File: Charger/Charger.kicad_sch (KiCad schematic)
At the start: 4 parts, among them J1 Bat_ballanser_conn, J2 Battery_conn, J3 Power_conn, J4 Screen_SPInCtrlnPwr_Conn

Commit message: Schematic trace update
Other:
- sheet MCU ports: added +3.3V; removed none
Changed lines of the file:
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@@
+		)
+	)
+	(wire
+		(pts
+			(xy 134.62 30.48) (xy 134.62 33.02)
+		)
+		(stroke
+			(width 0)
+			(type default)
 		)
 	)
@@
 		)
 	)
+	(symbol
+		(lib_id "power:+3.3V")
+		(at 134.62 30.48 0)
+		(unit 1)
+		(exclude_from_sim no)
+		(in_bom yes)
+		(on_board yes)
+		(dnp no)
+		(property "Reference" "#PWR067"
+			(at 134.62 34.29 0)
+			(effects
+				(font
+					(size 1.27 1.27)
+				)
+				(hide yes)
+			)
+		)
+		(property "Value" "+3.3V"
+			(at 134.62 26.67 0)
+			(effects
+				(font
+					(size 1.27 1.27)
+				)
+			)
+		)
+		(property "Footprint" ""
+			(at 134.62 30.48 0)
+			(effects
+				(font
+					(size 1.27 1.27)
+				)
+				(hide yes)
+			)
+		)
+		(property "Datasheet" ""
+			(at 134.62 30.48 0)
+			(effects
+				(font
+					(size 1.27 1.27)
+				)
+				(hide yes)
+			)
+		)
+		(property "Description" "Power symbol creates a global label with name \"+3.3V\""
+			(at 134.62 30.48 0)
+			(effects
+				(font
+					(size 1.27 1.27)
+				)
+				(hide yes)
+			)
+		)
+		(pin "1"
+		)
+		(instances
+			(project "Charger"
+				(path "/f0501846-9b00-4ec1-8596-952177c35a04"
+					(reference "#PWR067")
+					(unit 1)
+				)
+			)
+		)
+	)
 	(sheet
 		(at 214.63 114.3)
@@
 		(at 119.38 33.02)
 		(size 45.72 73.66)
-		(fields_autoplaced yes)
 		(stroke
 			(width 0.1524)
@@
 		)
 		(property "Sheetname" "MCU"
-			(at 119.38 32.3084 0)
-			(effects
-				(font
-					(size 1.27 1.27)
+			(at 139.954 71.12 0)
+			(effects
+				(font
+					(size 1.27 1.27)
+					(bold yes)
 				)
 				(justify left bottom)
@@
 			(effects
 				(font
+					(size 1.27 1.27)
+				)
+				(justify right)
+			)
+		)
+		(pin "+3.3V" input
+			(at 134.62 33.02 90)
+			(effects
+				(font

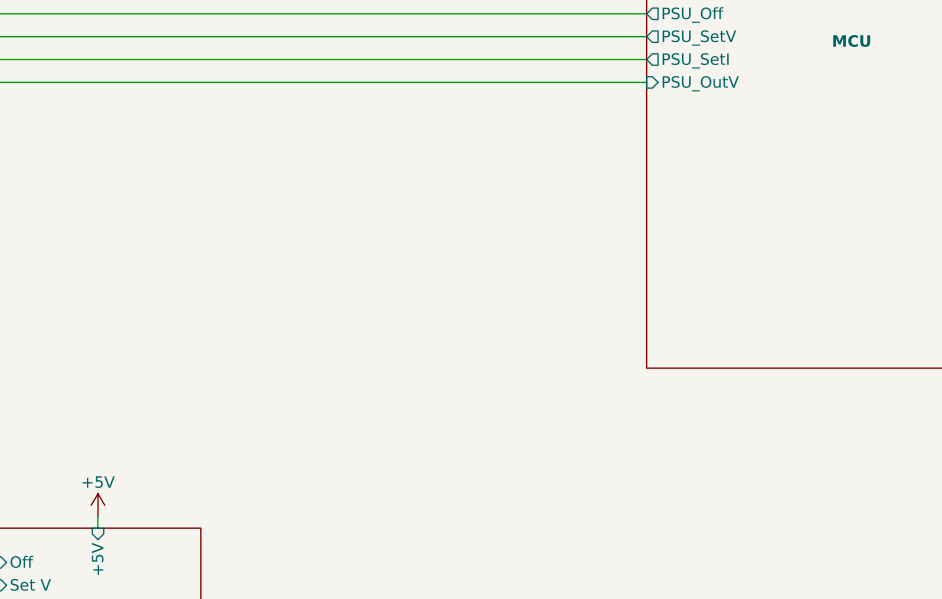
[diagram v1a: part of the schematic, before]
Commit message: Semi finished pinning the mcu and added ui pins
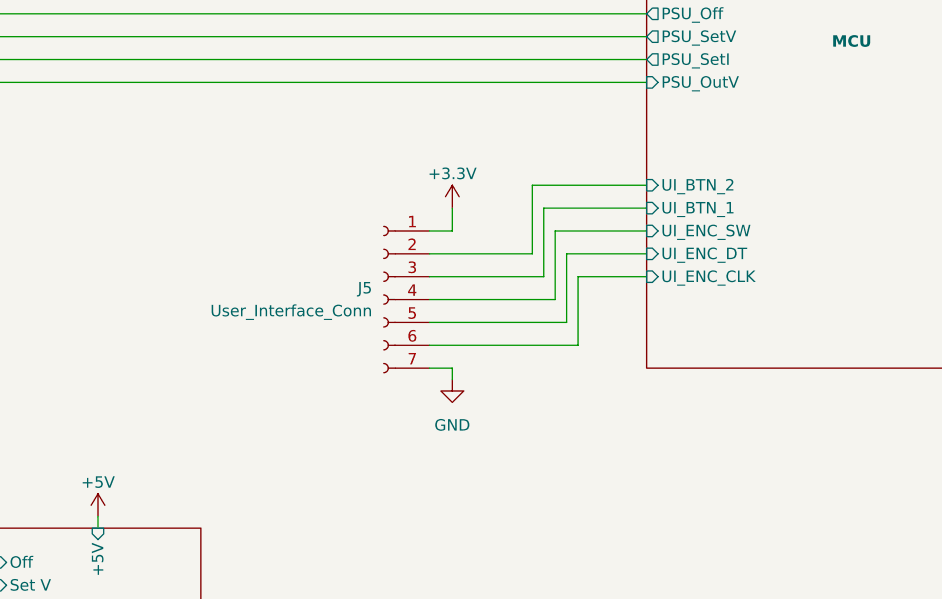
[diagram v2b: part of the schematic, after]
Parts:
- added J5: User_Interface_Conn, Connector_PinHeader_2.54mm:PinHeader_1x07_P2.54mm_Horizontal, symbol Connector:Conn_01x07_Socket
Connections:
- net +3.3V: now also J5.1 (Pin_1)
- net GND: now also J5.7 (Pin_7)
- new net MCU/UI_BTN_1: J5.3 (Pin_3)
- new net MCU/UI_BTN_2: J5.2 (Pin_2)
- new net MCU/UI_ENC_CLK: J5.6 (Pin_6)
- new net MCU/UI_ENC_DT: J5.5 (Pin_5)
- new net MCU/UI_ENC_SW: J5.4 (Pin_4)
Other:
- sheet MCU ports: added UI_BTN_1, UI_BTN_2, UI_ENC_CLK, UI_ENC_DT, UI_ENC_SW; removed none

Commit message: przegląd
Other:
- note added: "to jest załączenie baterii nie pomiaru"
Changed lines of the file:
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@@
+		)
+	)
+	(text "to jest załączenie baterii nie pomiaru \n"
+		(exclude_from_sim no)
+		(at 184.658 104.902 0)
+		(effects
+			(font
+				(size 1.27 1.27)
+			)
 		)
 	)

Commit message: Notes after design meeting
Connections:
- no-connect marks 0 -> 1
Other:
- note removed: "Co robi FM? xD"
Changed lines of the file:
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@@
 		(color 0 0 0 0)
+	)
+	(no_connect
+		(at 175.26 55.88)
 	)
 	(wire
@@
 		(effects
 			(font
-				(size 1.27 1.27)
-			)
-		)
-	)
-	(text "Co robi FM? xD"
-		(exclude_from_sim no)
-		(at 188.468 56.134 0)
-		(effects
-			(font

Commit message: UPDATE UC
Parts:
- added J7: Temp_Sens_Conn, Connector_PinHeader_2.54mm:PinHeader_1x02_P2.54mm_Vertical, symbol Connector:Conn_01x02_Socket
- J4: footprint (none) -> Connector_PinHeader_2.54mm:PinHeader_1x10_P2.54mm_Vertical
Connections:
- net GND: now also J7.1 (Pin_1)
- new net MCU/ONE_WIRE: J7.2 (Pin_2)
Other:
- sheet MCU ports: added BAT_P_ON, ONE_WIRE, PSU_OutI; removed ISENS_EN
- note added: "tu by chciały być magistrale"
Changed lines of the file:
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@@
 	(paper "A4")
 	(junction
+		(at 36.83 135.89)
+		(diameter 0)
+		(color 0 0 0 0)
+	)
+	(junction
 		(at 212.09 132.08)
 		(diameter 0)
@@
 	(wire
 		(pts
+			(xy 105.41 55.88) (xy 105.41 58.42)
+		)
+		(stroke
+			(width 0)
+			(type default)
+		)
+	)
+	(wire
+		(pts
 			(xy 171.45 35.56) (xy 175.26 35.56)
 		)
@@
 	(wire
 		(pts
+			(xy 119.38 77.47) (xy 27.94 77.47)
+		)
+		(stroke
+			(width 0)
+			(type default)
+		)
+	)
+	(wire
+		(pts
 			(xy 95.25 106.68) (xy 97.79 106.68)
 		)
@@
 	(wire
 		(pts
+			(xy 27.94 135.89) (xy 36.83 135.89)
+		)
+		(stroke
+			(width 0)
+			(type default)
+		)
+	)
+	(wire
+		(pts
 			(xy 110.49 93.98) (xy 119.38 93.98)
 		)
@@
 	(wire
 		(pts
+			(xy 101.6 53.34) (xy 119.38 53.34)
+		)
+		(stroke
+			(width 0)
+			(type default)
+		)
+	)
+	(wire
+		(pts
 			(xy 165.1 38.1) (xy 175.26 38.1)
 		)
@@
 	(wire
 		(pts
+			(xy 101.6 55.88) (xy 105.41 55.88)
+		)
+		(stroke
+			(width 0)
+			(type default)
+		)
+	)
+	(wire
+		(pts
 			(xy 95.25 96.52) (xy 107.95 96.52)
 		)
@@
 	(wire
 		(pts
+			(xy 27.94 77.47) (xy 27.94 135.89)
+		)
+		(stroke
+			(width 0)
+			(type default)
+		)
+	)
+	(wire
+		(pts
 			(xy 209.55 134.62) (xy 209.55 99.06)
 		)
@@
 		)
 	)
+	(text "tu by chciały być magistrale"
+		(exclude_from_sim no)
+		(at 92.964 66.04 0)
+		(effects
+			(font
+				(size 1.27 1.27)
+			)
+		)
+	)
 	(text "do sprawdzenia na bardzo poważnie czy hall jest dobrze włożony do schematu\n tzn jesli pchamy prąd do baterii to napiecie bedzie ponizej 1.65 a jesli \npobieramy z baterii to czy bedzie rosło"
 		(exclude_from_sim no)
@@
 	)
 	(symbol
+		(lib_id "Connector:Conn_01x02_Socket")
+		(at 96.52 55.88 180)
+		(unit 1)
+		(exclude_from_sim no)
+		(in_bom yes)
+		(on_board yes)
+		(dnp no)
+		(fields_autoplaced yes)
+		(property "Reference" "J7"
+			(at 97.155 48.26 0)
+			(effects
+				(font
+					(size 1.27 1.27)
+				)
+			)
+		)
+		(property "Value" "Temp_Sens_Conn"
+			(at 97.155 50.8 0)
+			(effects
+				(font
+					(size 1.27 1.27)
+				)
+			)
+		)
+		(property "Footprint" "Connector_PinHeader_2.54mm:PinHeader_1x02_P2.54mm_Vertical"
+			(at 96.52 55.88 0)
+			(effects
+				(font
+					(size 1.27 1.27)
+				)
+				(hide yes)
+			)
+		)
+		(property "Datasheet" "~"
+			(at 96.52 55.88 0)
+			(effects
+				(font
+					(size 1.27 1.27)
+				)
+				(hide yes)
+			)
+		)
+		(property "Description" "Generic connector, single row, 01x02, script generated"
+			(at 96.52 55.88 0)
+			(effects
+				(font
+					(size 1.27 1.27)
+				)
+				(hide yes)
+			)
+		)
+		(pin "1"
+		)
+		(pin "2"
+		)
+		(instances
+			(project "Charger"
+				(path "/f0501846-9b00-4ec1-8596-952177c35a04"
+					(reference "J7")
+					(unit 1)
+				)
+			)
+		)
+	)
+	(symbol
 		(lib_id "Connector:Conn_01x07_Socket")
 		(at 250.19 46.99 0)
@@
 			)
 		)
-		(property "Footprint" ""
+		(property "Footprint" "Connector_PinHeader_2.54mm:PinHeader_1x10_P2.54mm_Vertical"
 			(at 180.34 45.72 0)
 			(effects
@@
 	)
 	(symbol
+		(lib_id "power:GND")
+		(at 105.41 58.42 0)
+		(unit 1)
+		(exclude_from_sim no)
+		(in_bom yes)
+		(on_board yes)
+		(dnp no)
+		(property "Reference" "#PWR085"
+			(at 105.41 64.77 0)
+			(effects
+				(font
+					(size 1.27 1.27)
+				)
+				(hide yes)
+			)
+		)
+		(property "Value" "GND"
+			(at 105.41 62.738 0)
+			(effects
+				(font
+					(size 1.27 1.27)
+				)
+			)
+		)
+		(property "Footprint" ""
+			(at 105.41 58.42 0)
+			(effects
+				(font
+					(size 1.27 1.27)
+				)
+				(hide yes)
+			)
+		)
+		(property "Datasheet" ""
+			(at 105.41 58.42 0)
+			(effects
+				(font
+					(size 1.27 1.27)
+				)
+				(hide yes)
+			)
+		)
+		(property "Description" "Power symbol creates a global label with name \"GND\" , ground"
+			(at 105.41 58.42 0)
+			(effects
+				(font
+					(size 1.27 1.27)
+				)
+				(hide yes)
+			)
+		)
+		(pin "1"
+		)
+		(instances
+			(project "Charger"
+				(path "/f0501846-9b00-4ec1-8596-952177c35a04"
+					(reference "#PWR085")
+					(unit 1)
+				)
+			)
+		)
+	)
+	(symbol
 		(lib_id "power:+5V")
 		(at 223.52 114.3 0)
@@
 			)
 		)
-		(pin "ISENS_EN" output
-			(at 165.1 102.87 0)
-			(effects
-				(font
-					(size 1.27 1.27)
-				)
-				(justify right)
-			)
-		)
 		(pin "PSU_OutV" input
 			(at 119.38 74.93 180)
@@
 			)
 		)
+		(pin "PSU_OutI" input
+			(at 119.38 77.47 180)
+			(effects
+				(font
+					(size 1.27 1.27)
+				)
+				(justify left)
+			)
+		)
+		(pin "ONE_WIRE" output
+			(at 119.38 53.34 180)
+			(effects
+				(font
+					(size 1.27 1.27)
+				)
+				(justify left)
+			)
+		)
+		(pin "BAT_P_ON" output
+			(at 165.1 102.87 0)
+			(effects
+				(font
+					(size 1.27 1.27)
+				)
+				(justify right)
+			)
+		)

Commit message: pcb up
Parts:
- removed J7: Temp_Sens_Conn, Connector_PinHeader_2.54mm:PinHeader_1x02_P2.54mm_Vertical, symbol Connector:Conn_01x02_Socket
- added D7: SS26, Diode_SMD:D_SMA, symbol Diode:SS26
- added F1, F2: Fuse_Small, Fuse:Fuse_2010_5025Metric_Pad1.52x2.65mm_HandSolder, symbol Device:Fuse_Small
- added J8: Temp_Sens_Conn, Connector_PinHeader_2.54mm:PinHeader_1x03_P2.54mm_Vertical, symbol Connector:Conn_01x03_Socket
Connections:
- net Zasilacz/Z- is gone; now on net GND: J3.1 (Pin_1)
- net +3.3V: now also J8.3 (Pin_3)
- net GND: now also D7.2 (A), J8.1 (Pin_1)
- net Ladowarka/Vout: now also F2.1
- net MCU/ONE_WIRE: now also J8.2 (Pin_2)
- net Ladowarka/Vin: no longer names the net of J3.2 (Pin_2)
- net Ladowarka/Vin: now also F1.1
- new net +36V: D7.1 (K), F1.2
- new net Sztuczne_obciazenie/B+: F2.2
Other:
- note removed: "to jest załączenie baterii nie pomiaru"
- moved on the sheet: J3

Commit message: small update
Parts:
- F1: value Fuse_Small -> 10A
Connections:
- net MCU/SPI_CS: now also J4.3 (Pin_3); no longer J4.4 (Pin_4)
- net MCU/SPI_MISO: now also J4.2 (Pin_2); no longer J4.3 (Pin_3)
- net MCU/SPI_MOSI: now also J4.5 (Pin_5); no longer J4.2 (Pin_2)
- net MCU/SPI_SCK: now also J4.4 (Pin_4); no longer J4.5 (Pin_5)
- net MCU/UI_BTN_1: now also J5.2 (Pin_2); no longer J5.3 (Pin_3)
- net MCU/UI_BTN_2: now also J5.3 (Pin_3); no longer J5.2 (Pin_2)
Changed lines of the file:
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@@
 			)
 		)
-		(property "Value" "Fuse_Small"
+		(property "Value" "10A"
 			(at 33.02 44.45 0)
 			(effects
@@
 		)
 		(pin "SPI_SCK" output
+			(at 165.1 43.18 0)
+			(effects
+				(font
+					(size 1.27 1.27)
+				)
+				(justify right)
+			)
+		)
+		(pin "SPI_CS" output
+			(at 165.1 40.64 0)
+			(effects
+				(font
+					(size 1.27 1.27)
+				)
+				(justify right)
+			)
+		)
+		(pin "SPI_MISO" input
+			(at 165.1 38.1 0)
+			(effects
+				(font
+					(size 1.27 1.27)
+				)
+				(justify right)
+			)
+		)
+		(pin "SPI_MOSI" output
 			(at 165.1 45.72 0)
-			(effects
-				(font
-					(size 1.27 1.27)
-				)
-				(justify right)
-			)
-		)
-		(pin "SPI_CS" output
-			(at 165.1 43.18 0)
-			(effects
-				(font
-					(size 1.27 1.27)
-				)
-				(justify right)
-			)
-		)
-		(pin "SPI_MISO" input
-			(at 165.1 40.64 0)
-			(effects
-				(font
-					(size 1.27 1.27)
-				)
-				(justify right)
-			)
-		)
-		(pin "SPI_MOSI" output
-			(at 165.1 38.1 0)
 			(effects
 				(font
@@
 		)
 		(pin "UI_BTN_2" input
+			(at 119.38 88.9 180)
+			(effects
+				(font
+					(size 1.27 1.27)
+				)
+				(justify left)
+			)
+		)
+		(pin "UI_BTN_1" input
 			(at 119.38 86.36 180)
 			(effects
 				(font
-					(size 1.27 1.27)
-				)
-				(justify left)
-			)
-		)
-		(pin "UI_BTN_1" input
-			(at 119.38 88.9 180)
-			(effects
-				(font

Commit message: pcb poukladane
usuniete 3 kondensatory
brak poligonow i odprowadzania ciepla
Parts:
- J5: footprint Connector_PinHeader_2.54mm:PinHeader_1x07_P2.54mm_Horizontal -> Connector_PinHeader_2.54mm:PinHeader_1x07_P2.54mm_Vertical
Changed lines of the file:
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@@
 			)
 		)
-		(property "Footprint" "Connector_PinHeader_2.54mm:PinHeader_1x07_P2.54mm_Horizontal"
+		(property "Footprint" "Connector_PinHeader_2.54mm:PinHeader_1x07_P2.54mm_Vertical"
 			(at 90.17 99.06 0)
 			(effects
